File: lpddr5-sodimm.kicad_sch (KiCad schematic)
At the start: 3 parts, among them Q1 DMG1012T-7

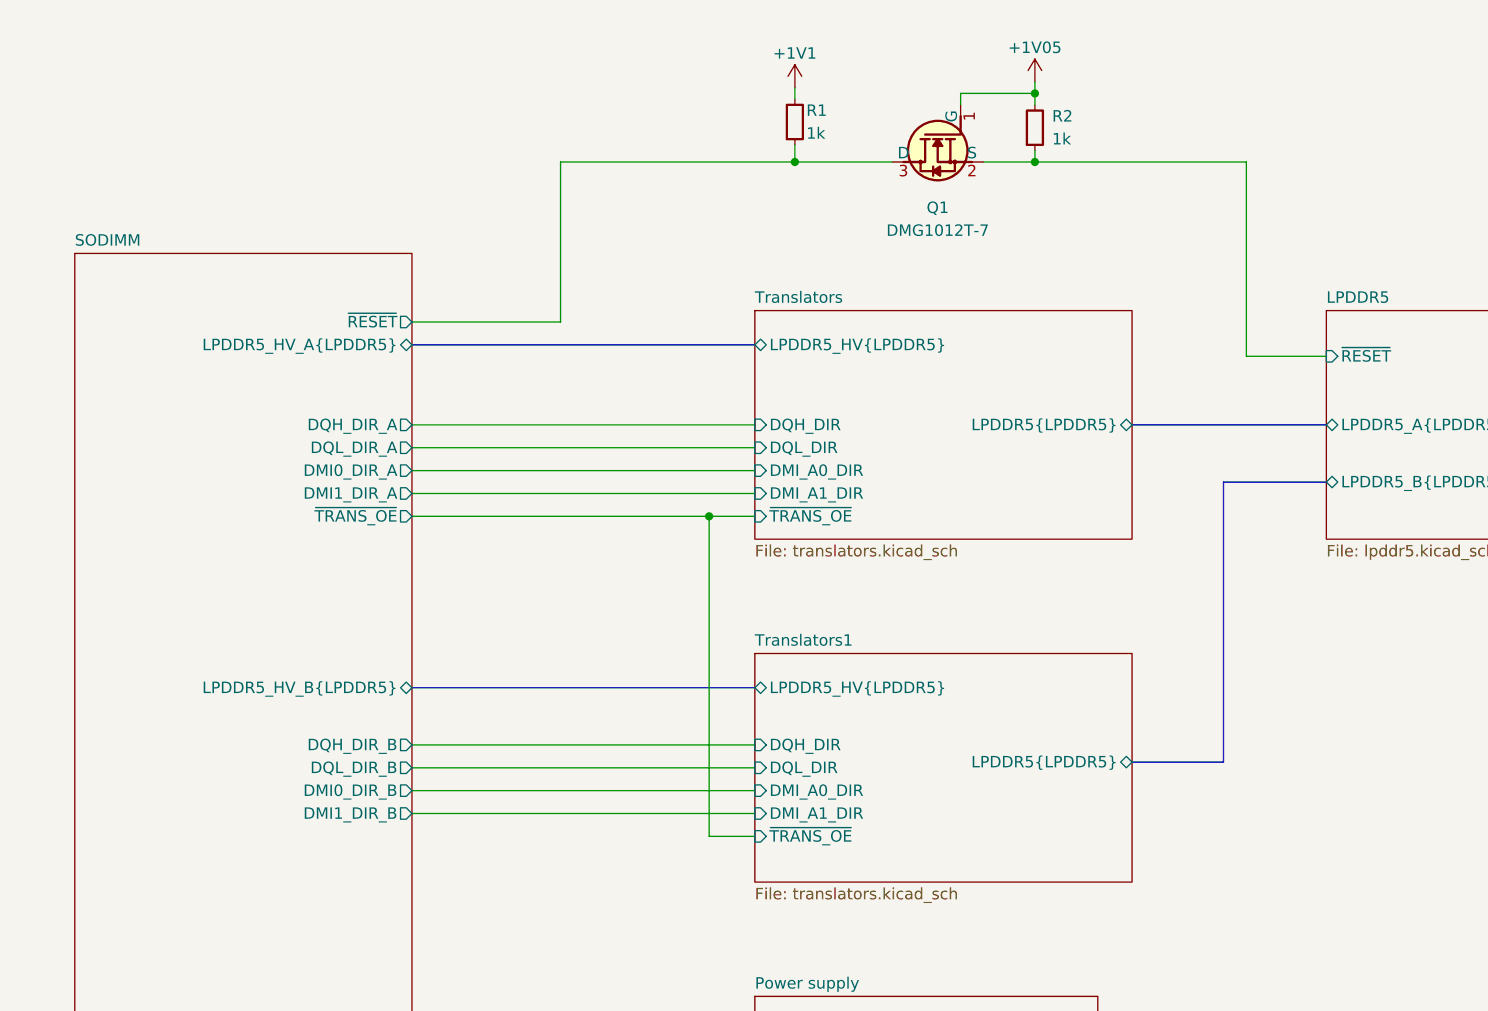
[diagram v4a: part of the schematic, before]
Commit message: [#52536] 52835: use resistors dividers instead of translators
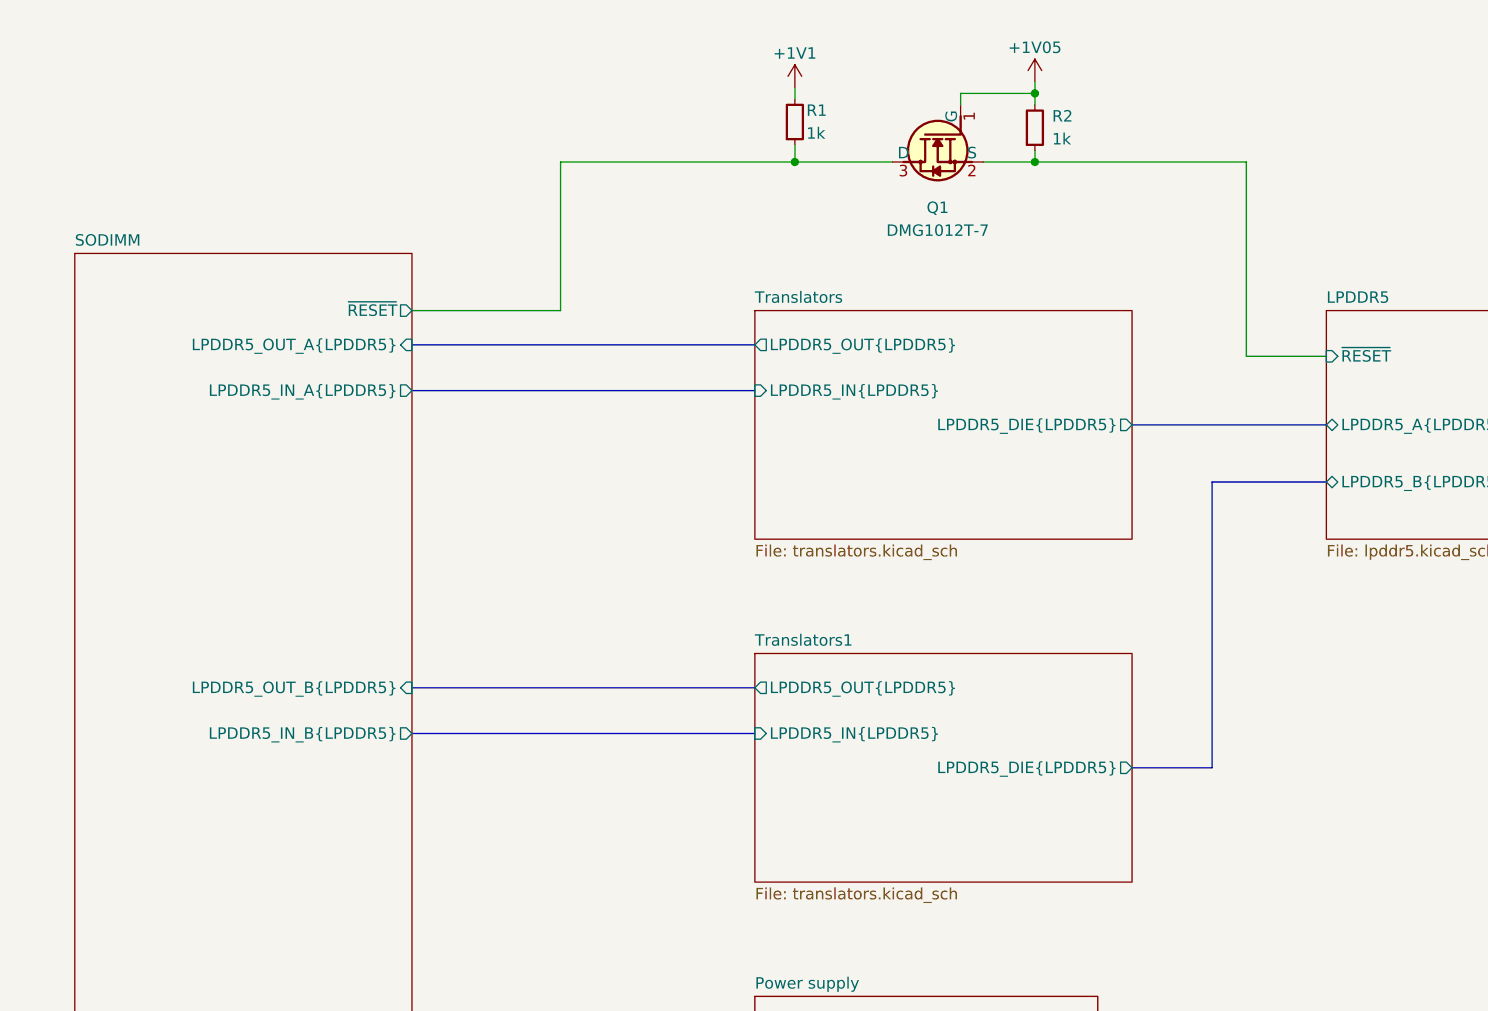
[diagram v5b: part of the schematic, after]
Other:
- sheet SODIMM ports: added LPDDR5_IN_A{LPDDR5}, LPDDR5_IN_B{LPDDR5}, LPDDR5_OUT_A{LPDDR5}, LPDDR5_OUT_B{LPDDR5}; removed DMI0_DIR_A, DMI0_DIR_B, DMI1_DIR_A, DMI1_DIR_B, DQH_DIR_A, DQH_DIR_B, DQL_DIR_A, DQL_DIR_B, LPDDR5_HV_A{LPDDR5}, LPDDR5_HV_B{LPDDR5}, ~{TRANS_OE}
- sheet Translators ports: added LPDDR5_DIE{LPDDR5}, LPDDR5_IN{LPDDR5}, LPDDR5_OUT{LPDDR5}; removed DMI_A0_DIR, DMI_A1_DIR, DQH_DIR, DQL_DIR, LPDDR5_HV{LPDDR5}, LPDDR5{LPDDR5}, ~{TRANS_OE}
- sheet Translators1 ports: added LPDDR5_DIE{LPDDR5}, LPDDR5_IN{LPDDR5}, LPDDR5_OUT{LPDDR5}; removed DMI_A0_DIR, DMI_A1_DIR, DQH_DIR, DQL_DIR, LPDDR5_HV{LPDDR5}, LPDDR5{LPDDR5}, ~{TRANS_OE}

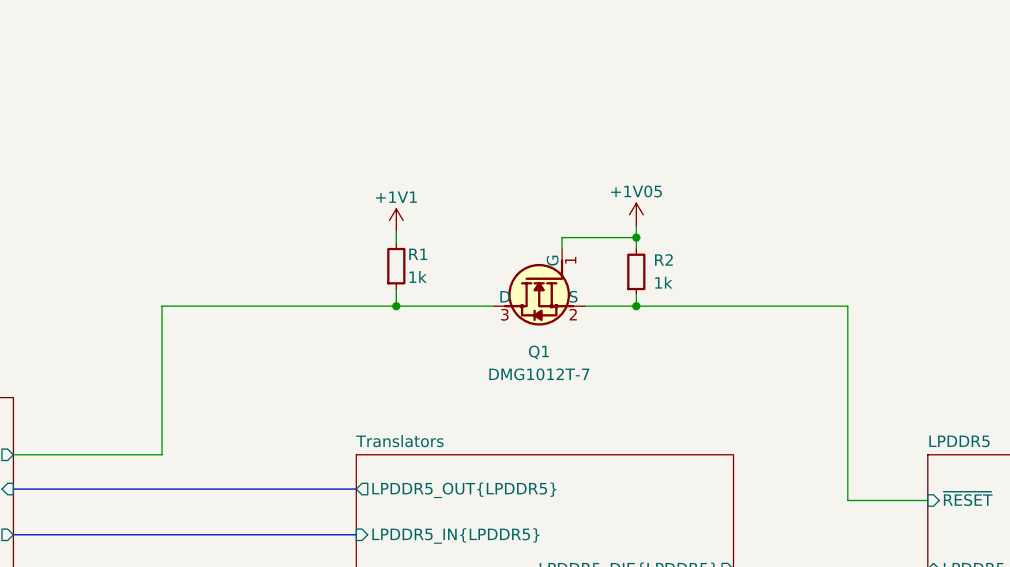
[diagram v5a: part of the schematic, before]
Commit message: [#52835] schematics: replace array resistors with 0402
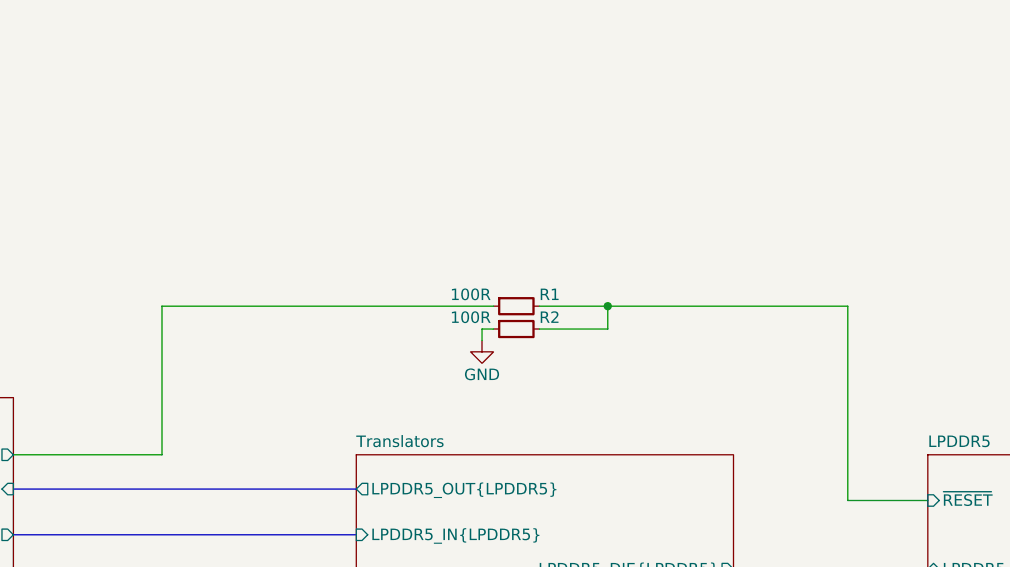
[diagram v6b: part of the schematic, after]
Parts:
- removed Q1: DMG1012T-7, antmicro-footprints:SOT-523, symbol antmicroTransistorsFETsMOSFETsSingle:DMG1012T-7
- removed R1, R2: R_1k_0402, antmicro-footprints:R_0402_1005Metric, symbol antmicroResistors0402:R_1k_0402
- added R1, R2: R_100R_0402, antmicro-footprints:R_0402_1005Metric, symbol antmicroResistors0402:R_100R_0402
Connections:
- net LPDDR5/~{RESET}: now also R1.2, R2.2
- net SODIMM/~{RESET}: now also R1.1
- new net GND: R2.1
